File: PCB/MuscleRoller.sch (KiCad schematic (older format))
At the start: 26 parts, among them J19 Conn_01x04_Male, J3 Screw_Terminal_01x02, J4 Conn_02x03_Odd_Even, J5 Conn_02x03_Odd_Even, J6 Conn_01x03_Male, J7 Conn_01x04_Male, U1 AZ1117-3.3, U2 ESP32-S2-WROOM

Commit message: PCB complete
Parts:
- added J11, J12: Conn_01x03_Male, Connector_JST:JST_XH_B3B-XH-A_1x03_P2.50mm_Vertical, symbol Connector:Conn_01x03_Male
- R4: value 47K -> 10K
- gave numbers to parts that had none: 4
- renumbered J3 to J1, J4 to J2, J5 to J3, J19 to J4, J7 to J9
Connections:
- net DAC1 is gone; now on net LC_DAT2: U2.20 (IO17)
- net +3V3: now also J11.1 (Pin_1), J12.1 (Pin_1)
- net CHARGE: now also U2.13 (IO10); no longer U2.16 (IO13)
- net DIRX: now also U2.14 (IO11); no longer U2.17 (IO14)
- net ENX: now also U2.16 (IO13); no longer U2.19 (IO16)
- net ENZ: now also U2.12 (IO9); no longer U2.15 (IO12)
- net GND: now also J11.2 (Pin_2), J12.2 (Pin_2)
- net LC_CLK: now also U2.17 (IO14); no longer U2.6 (IO3)
- net LC_CLK2: now also U2.19 (IO16); no longer U2.8 (IO5)
- net LC_DAT: now also U2.18 (IO15); no longer U2.7 (IO4)
- net LC_DAT2: no longer U2.9 (IO6)
- net STEPX: now also U2.15 (IO12); no longer U2.18 (IO15)
- net HOMZ: now reaches U2.27 (IO33)
- net HOMZ: now also J12.3 (Pin_3)
- net HOMX: now reaches U2.28 (IO34)
- net HOMX: now also J11.3 (Pin_3)

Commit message: PCB order
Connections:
- net XA1: now also J9.3 (Pin_3); no longer J9.4 (Pin_4)
- net XA2: now also J9.4 (Pin_4); no longer J9.3 (Pin_3)
- net ZA1: now also J10.3 (Pin_3); no longer J10.4 (Pin_4)
- net ZA2: now also J10.4 (Pin_4); no longer J10.3 (Pin_3)
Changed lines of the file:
@@
 Text GLabel 3850 4900 0    50   Input ~ 0
 XB2
+Text GLabel 4550 4700 0    50   Input ~ 0
+XA1
 Text GLabel 4550 4600 0    50   Input ~ 0
-XA1
-Text GLabel 4550 4700 0    50   Input ~ 0
 XA2
 Text GLabel 4550 4800 0    50   Input ~ 0
@@
 Text GLabel 3850 7000 0    50   Input ~ 0
 ZB2
+Text GLabel 4550 6800 0    50   Input ~ 0
+ZA1
 Text GLabel 4550 6700 0    50   Input ~ 0
-ZA1
-Text GLabel 4550 6800 0    50   Input ~ 0
 ZA2
 Text GLabel 4550 6900 0    50   Input ~ 0

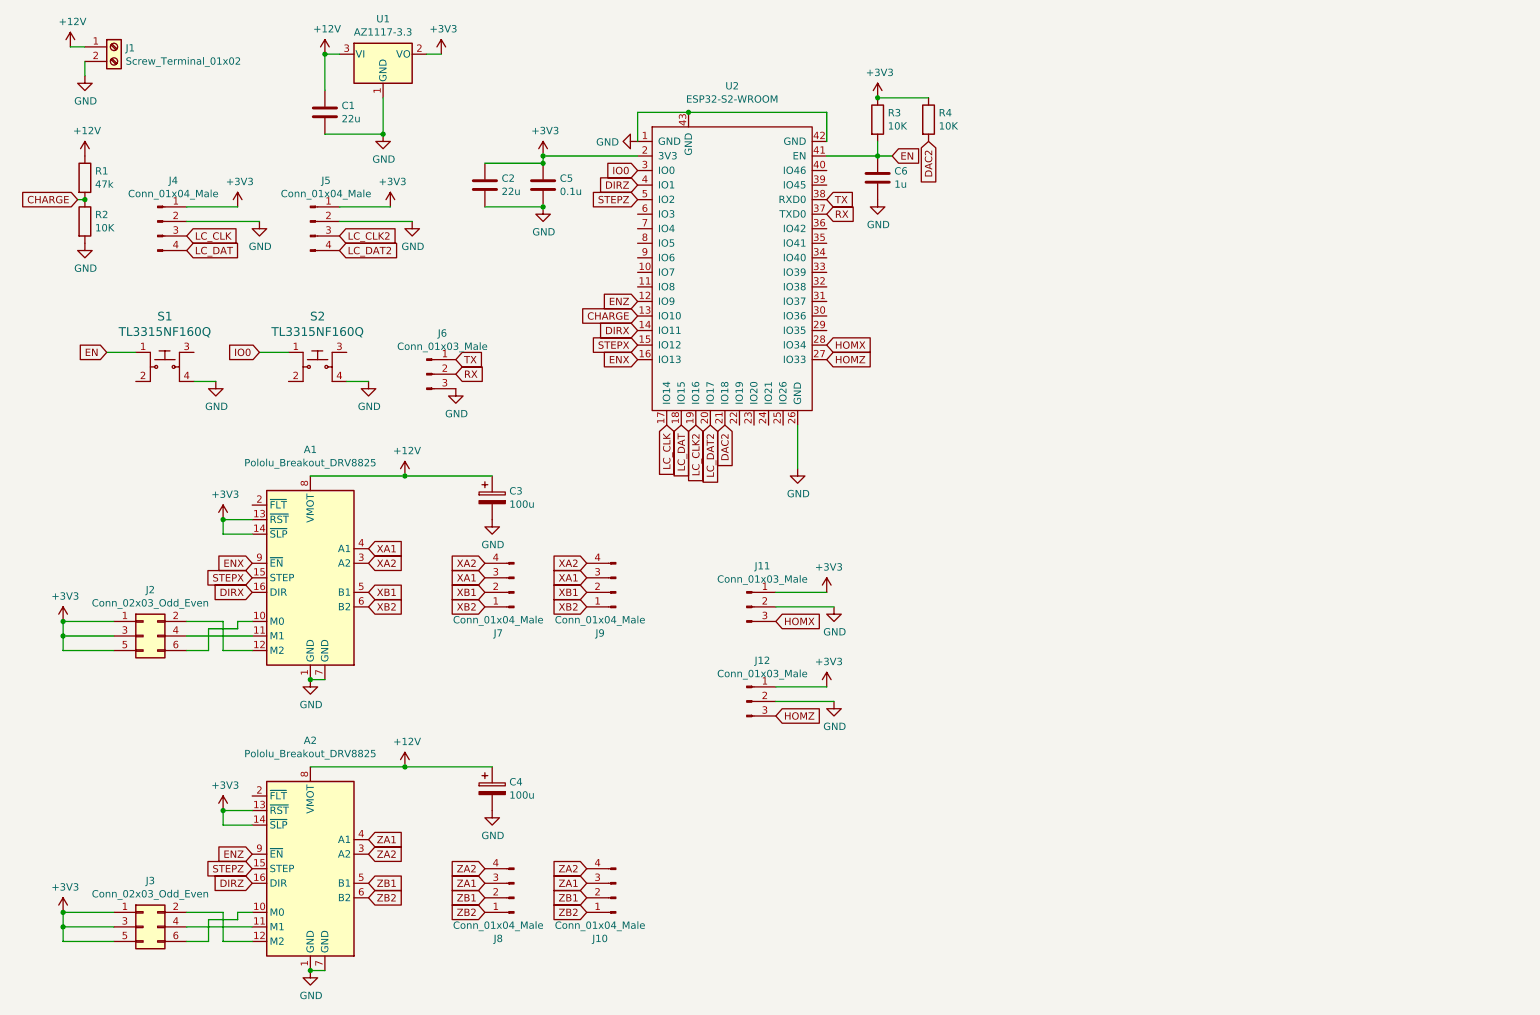
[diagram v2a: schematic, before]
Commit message: switch to ESP32 from ESP32-S2 for bluetooth
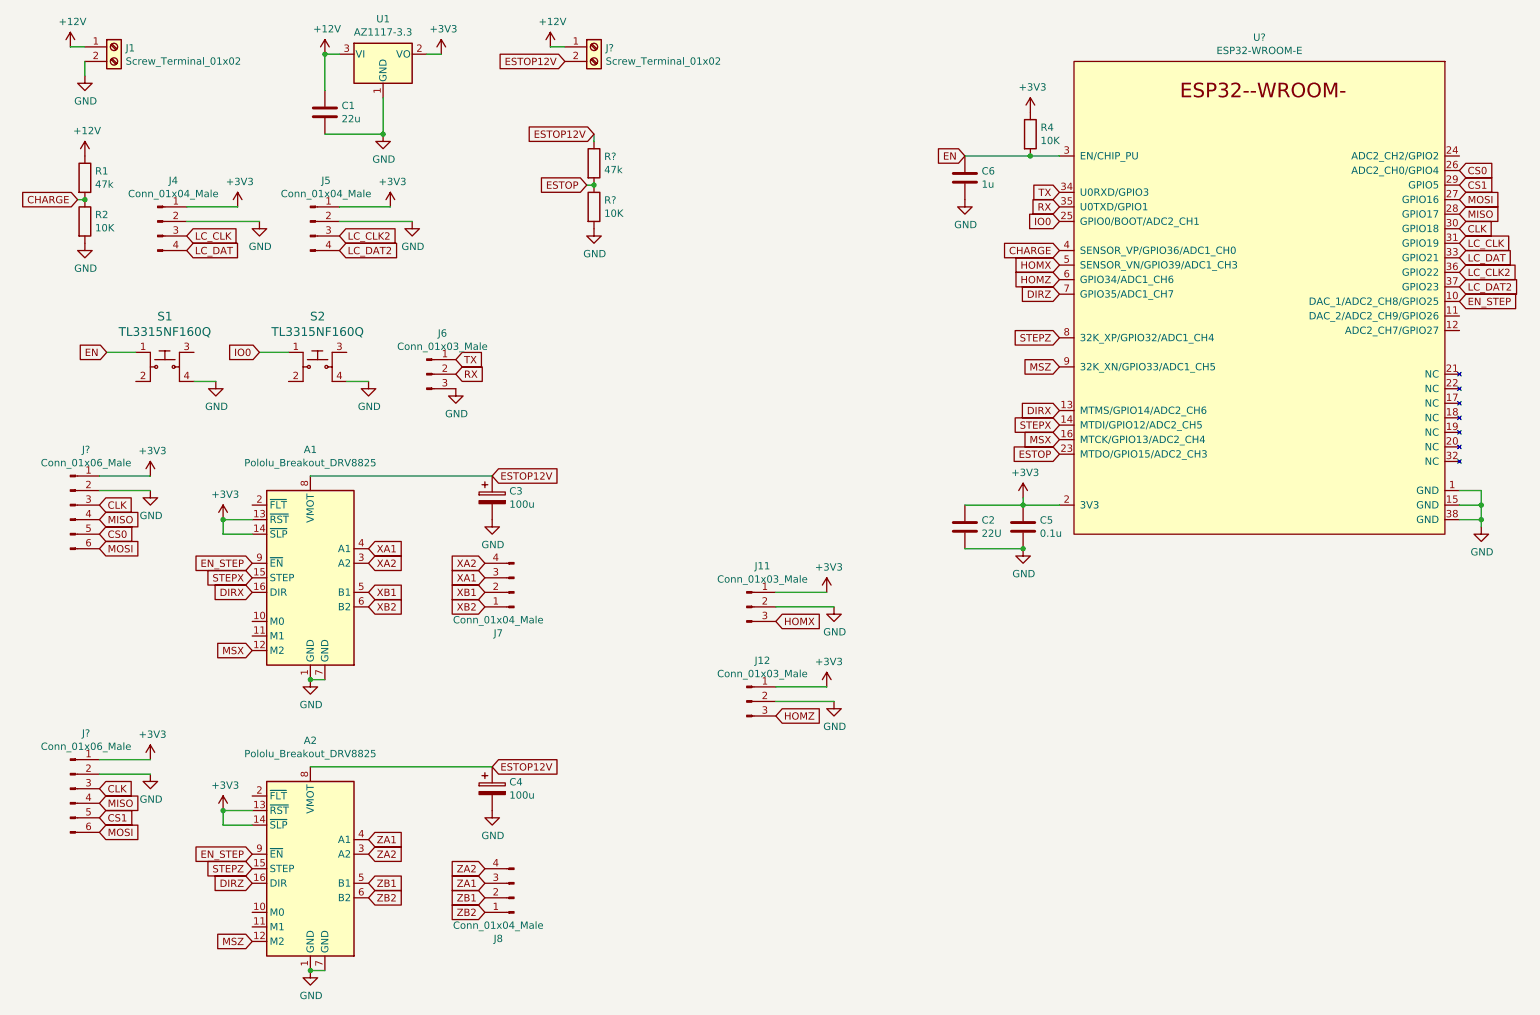
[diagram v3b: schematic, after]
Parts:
- removed J10, J9: Conn_01x04_Male, Connector_JST:JST_XH_B4B-XH-A_1x04_P2.50mm_Vertical, symbol Connector:Conn_01x04_Male
- removed J2, J3: Conn_02x03_Odd_Even, Connector_PinHeader_2.54mm:PinHeader_2x03_P2.54mm_Vertical, symbol Connector_Generic:Conn_02x03_Odd_Even
- removed R3: 10K, Resistor_SMD:R_0805_2012Metric_Pad1.20x1.40mm_HandSolder, symbol Device:R
- removed U2: ESP32-S2-WROOM, A4:ESP32-S2-WROOM, symbol A4:ESP32-S2-WROOM
- added J?: Screw_Terminal_01x02, TerminalBlock_Phoenix:TerminalBlock_Phoenix_MKDS-1,5-2_1x02_P5.00mm_Horizontal, symbol Connector:Screw_Terminal_01x02
- added J? (x2): Conn_01x06_Male, Connector_JST:JST_XH_B6B-XH-A_1x06_P2.50mm_Vertical, symbol Connector:Conn_01x06_Male
- added R?: 47k, Resistor_SMD:R_0805_2012Metric_Pad1.20x1.40mm_HandSolder, symbol Device:R
- added R?: 10K, Resistor_SMD:R_0805_2012Metric_Pad1.20x1.40mm_HandSolder, symbol Device:R
- added U?: ESP32-WROOM-E, Espressif:ESP32-WROOM-32E, symbol Espressif:ESP32-WROOM-E
- C2: value 22u -> 22U
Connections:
- net DAC2 is gone; now on net EN: R4.2
- net ENZ is gone; now on net EN_STEP: A2.9 (~EN)
- net +12V: now also J?.1 (Pin_1); no longer A1.8 (VMOT), A2.8 (VMOT), C3.1, C4.1
- net +3V3: now also J?.1 (Pin_1), J?.1 (Pin_1), U?.2 (3V3)
- net CHARGE: now also U?.4 (SENSOR_VP/GPIO36/ADC1_CH0)
- net DIRX: now also U?.13 (MTMS/GPIO14/ADC2_CH6)
- net DIRZ: now also U?.7 (GPIO35/ADC1_CH7)
- net EN: now also U?.3 (EN/CHIP_PU)
- net GND: now also J?.2 (Pin_2), J?.2 (Pin_2), R?.2, U?.1 (GND), U?.15 (GND), U?.38 (GND)
- net HOMX: now also U?.5 (SENSOR_VN/GPIO39/ADC1_CH3)
- net HOMZ: now also U?.6 (GPIO34/ADC1_CH6)
- net IO0: now also U?.25 (GPIO0/BOOT/ADC2_CH1)
- net LC_CLK: now also U?.31 (GPIO19)
- net LC_CLK2: now also U?.36 (GPIO22)
- net LC_DAT: now also U?.33 (GPIO21)
- net LC_DAT2: now also U?.37 (GPIO23)
- net RX: now also U?.35 (U0TXD/GPIO1)
- net STEPX: now also U?.14 (MTDI/GPIO12/ADC2_CH5)
- net STEPZ: now also U?.8 (32K_XP/GPIO32/ADC1_CH4)
- net TX: now also U?.34 (U0RXD/GPIO3)
- net MSX: now reaches A1.12 (M2)
- net MSX: now also U?.16 (MTCK/GPIO13/ADC2_CH4)
- net MSZ: now reaches A2.12 (M2)
- net MSZ: now also U?.9 (32K_XN/GPIO33/ADC1_CH5)
- net ENX renamed EN_STEP
- net EN_STEP: now also U?.10 (DAC_1/ADC2_CH8/GPIO25)
- new net CLK: J?.3 (Pin_3), J?.3 (Pin_3), U?.30 (GPIO18)
- new net CS0: J?.5 (Pin_5), U?.26 (ADC2_CH0/GPIO4)
- new net CS1: J?.5 (Pin_5), U?.29 (GPIO5)
- new net ESTOP: R?.1, R?.2, U?.23 (MTDO/GPIO15/ADC2_CH3)
- new net ESTOP12V: A1.8 (VMOT), A2.8 (VMOT), C3.1, C4.1, J?.2 (Pin_2), R?.1
- new net MISO: J?.4 (Pin_4), J?.4 (Pin_4), U?.28 (GPIO17)
- new net MOSI: J?.6 (Pin_6), J?.6 (Pin_6), U?.27 (GPIO16)
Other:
- moved on the sheet: C2, R4

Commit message: PCB complete
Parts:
- gave numbers to parts that had none: 6
- renumbered C3 to C2, C4 to C3, C6 to C4, C2 to C5, C5 to C6, J11 to J10, J12 to J11, J1 to J3, R4 to R5
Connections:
- net CLK: now also U2.26 (ADC2_CH0/GPIO4); no longer U2.30 (GPIO18)
- net CS0: now also U2.28 (GPIO17); no longer U2.26 (ADC2_CH0/GPIO4)
- net CS1: now also U2.30 (GPIO18); no longer U2.29 (GPIO5)
- net DIRX: now also U2.5 (SENSOR_VN/GPIO39/ADC1_CH3); no longer U2.13 (MTMS/GPIO14/ADC2_CH6)
- net DIRZ: now also U2.9 (32K_XN/GPIO33/ADC1_CH5); no longer U2.7 (GPIO35/ADC1_CH7)
- net EN_STEP: now also U2.8 (32K_XP/GPIO32/ADC1_CH4); no longer U2.10 (DAC_1/ADC2_CH8/GPIO25)
- net HOMX: now also U2.33 (GPIO21); no longer U2.5 (SENSOR_VN/GPIO39/ADC1_CH3)
- net HOMZ: now also U2.31 (GPIO19); no longer U2.6 (GPIO34/ADC1_CH6)
- net LC_CLK: now also U2.12 (ADC2_CH7/GPIO27); no longer U2.31 (GPIO19)
- net LC_CLK2: now also U2.14 (MTDI/GPIO12/ADC2_CH5); no longer U2.36 (GPIO22)
- net LC_DAT: now also U2.13 (MTMS/GPIO14/ADC2_CH6); no longer U2.33 (GPIO21)
- net LC_DAT2: now also U2.16 (MTCK/GPIO13/ADC2_CH4); no longer U2.37 (GPIO23)
- net MISO: now also U2.27 (GPIO16); no longer U2.28 (GPIO17)
- net MOSI: now also U2.29 (GPIO5); no longer U2.27 (GPIO16)
- net MSX: now also U2.7 (GPIO35/ADC1_CH7); no longer U2.16 (MTCK/GPIO13/ADC2_CH4)
- net MSZ: now also U2.11 (DAC_2/ADC2_CH9/GPIO26); no longer U2.9 (32K_XN/GPIO33/ADC1_CH5)
- net STEPX: now also U2.6 (GPIO34/ADC1_CH6); no longer U2.14 (MTDI/GPIO12/ADC2_CH5)
- net STEPZ: now also U2.10 (DAC_1/ADC2_CH8/GPIO25); no longer U2.8 (32K_XP/GPIO32/ADC1_CH4)

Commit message: encoders working
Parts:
- U2: symbol Espressif:ESP32-WROOM-E -> MuscleRoller-rescue:ESP32-WROOM-E-Espressif
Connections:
- net DIRX: now also U2.37 (GPIO23); no longer U2.5 (SENSOR_VN/GPIO39/ADC1_CH3)
- net ESTOP: now also U2.5 (SENSOR_VN/GPIO39/ADC1_CH3); no longer U2.23 (MTDO/GPIO15/ADC2_CH3)
- net MSX: now also U2.23 (MTDO/GPIO15/ADC2_CH3); no longer U2.7 (GPIO35/ADC1_CH7)
- net STEPX: now also U2.36 (GPIO22); no longer U2.6 (GPIO34/ADC1_CH6)
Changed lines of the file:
@@
 	7150 4500 7550 4500
 Connection ~ 7550 4500
-Text GLabel 7800 2650 0    50   Input ~ 0
+Text GLabel 10550 2600 2    50   Input ~ 0
 STEPX
-Text GLabel 7800 2550 0    50   Input ~ 0
+Text GLabel 10550 2700 2    50   Input ~ 0
 DIRX
 Text GLabel 7800 3250 0    50   Input ~ 0
@@
 	1    0    0    -1
 $EndComp
-Text GLabel 7800 3850 0    50   Input ~ 0
+Text GLabel 7800 2550 0    50   Input ~ 0
 ESTOP
 Text GLabel 2300 3150 0    50   Input ~ 0
@@
 Text GLabel 10550 2900 2    50   Input ~ 0
 MSZ
-Text GLabel 7800 2750 0    50   Input ~ 0
+Text GLabel 7800 3850 0    50   Input ~ 0
 MSX
 $Comp
-L Espressif:ESP32-WROOM-E U2
+L MuscleRoller-rescue:ESP32-WROOM-E-Espressif U2
 U 1 1 61EA4056
 P 9150 2800

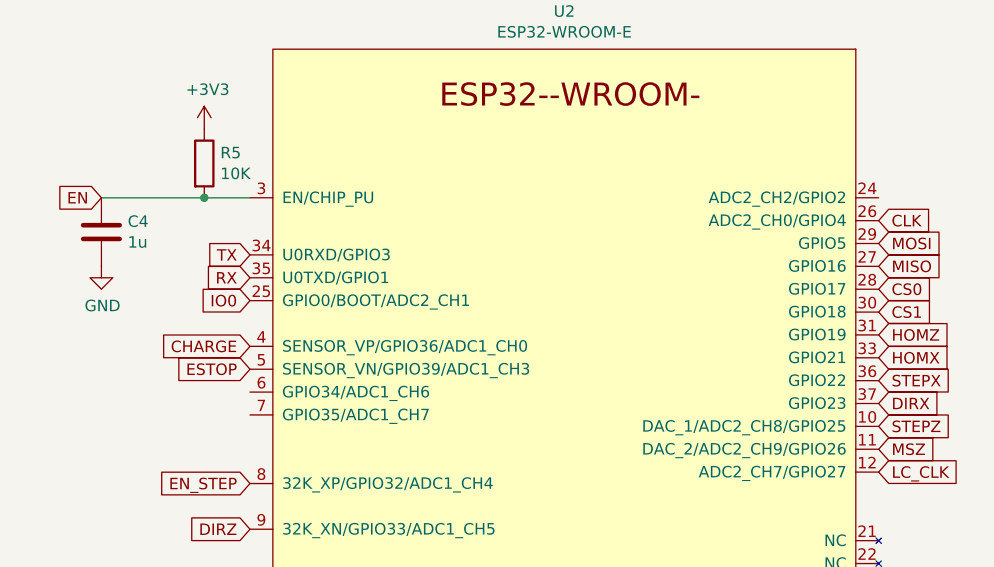
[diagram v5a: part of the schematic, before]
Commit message: GPIO pin updates complete
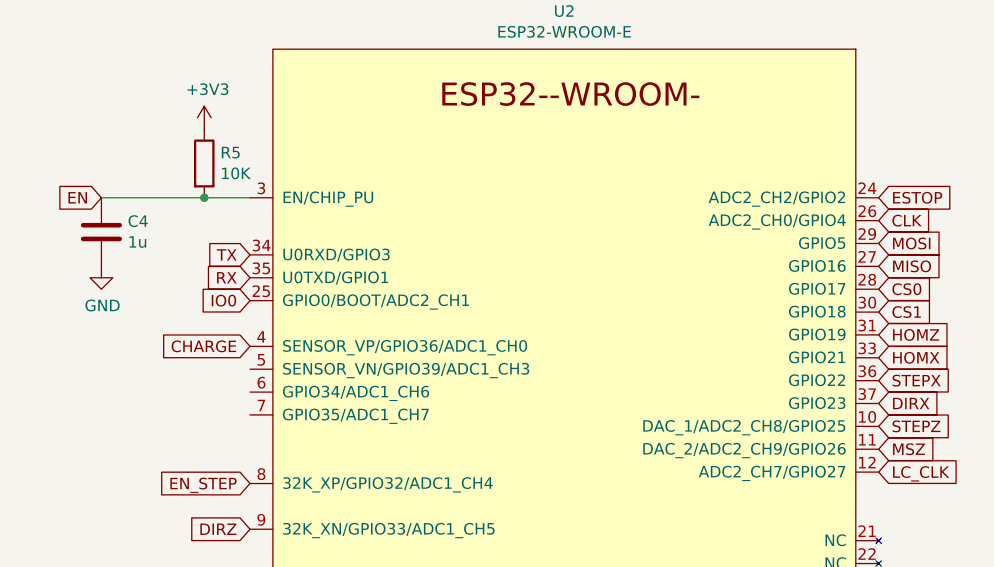
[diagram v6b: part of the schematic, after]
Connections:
- net ESTOP: now also U2.24 (ADC2_CH2/GPIO2); no longer U2.5 (SENSOR_VN/GPIO39/ADC1_CH3)
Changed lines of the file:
@@
 	1    0    0    -1
 $EndComp
-Text GLabel 7800 2550 0    50   Input ~ 0
+Text GLabel 10550 1800 2    50   Input ~ 0
 ESTOP
 Text GLabel 2300 3150 0    50   Input ~ 0
